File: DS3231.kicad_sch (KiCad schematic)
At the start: 8 parts, among them IC2 DS3231, J4 Conn_01x08_Pin

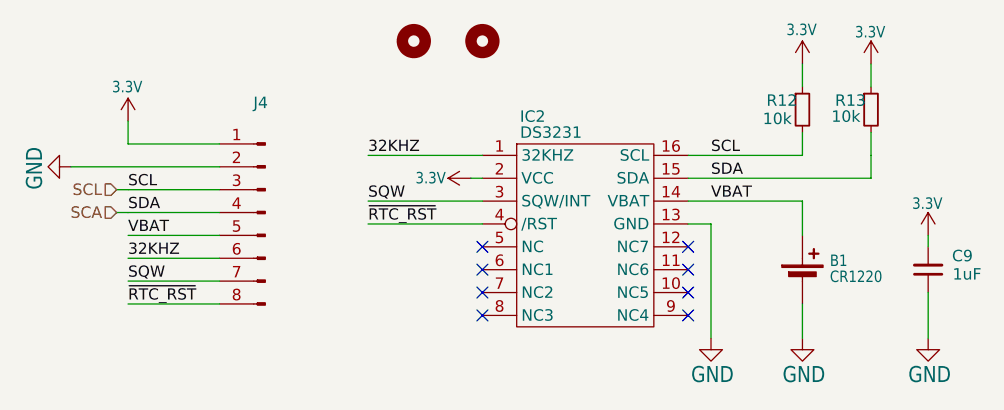
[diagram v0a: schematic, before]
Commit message: added pyrano, anemo, AM2315C, power supply, LEDs, switch and FPC connector in schematic
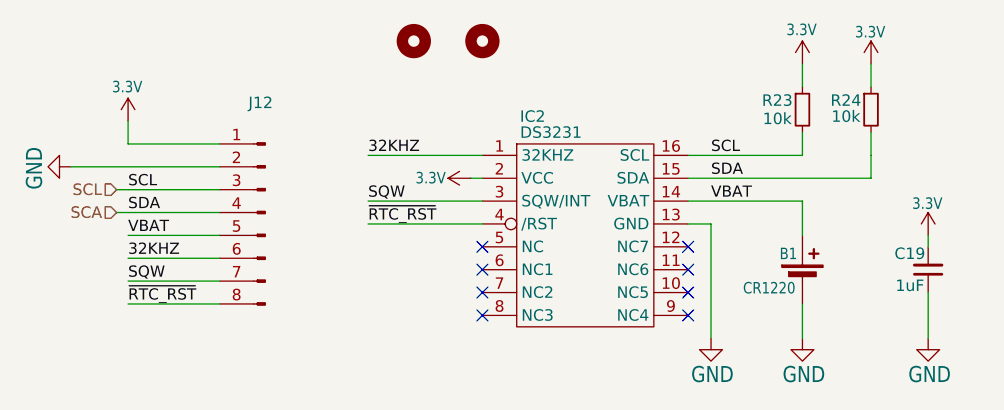
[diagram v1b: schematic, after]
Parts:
- renumbered C9 to C19, J4 to J12, R12 to R23, R13 to R24, U$6 to U$10, U$5 to U$9
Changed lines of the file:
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@@
 		(on_board yes)
 		(dnp no)
-		(property "Reference" "R13"
-			(at 180.594 81.534 0)
+		(property "Reference" "R24"
+			(at 180.086 81.534 0)
 			(effects
 				(font
@@
 			(project "testing-station"
 				(path "/ed3950ec-e24f-4dd6-b9cc-eca012f1333b/7b5dd94c-543e-4c31-b2c6-5bdcb1b32a26"
-					(reference "R13")
+					(reference "R24")
 					(unit 1)
 				)
@@
 		(on_board yes)
 		(dnp no)
-		(property "Reference" "U$6"
+		(property "Reference" "U$10"
 			(at 139.7 74.93 0)
 			(effects
@@
 			(project "testing-station"
 				(path "/ed3950ec-e24f-4dd6-b9cc-eca012f1333b/7b5dd94c-543e-4c31-b2c6-5bdcb1b32a26"
-					(reference "U$6")
+					(reference "U$10")
 					(unit 1)
 				)
@@
 		(on_board yes)
 		(dnp no)
-		(property "Reference" "#U$037"
+		(property "Reference" "#U$067"
 			(at 189.23 96.52 0)
 			(effects
@@
 			(project "testing-station"
 				(path "/ed3950ec-e24f-4dd6-b9cc-eca012f1333b/7b5dd94c-543e-4c31-b2c6-5bdcb1b32a26"
-					(reference "#U$037")
+					(reference "#U$067")
 					(unit 1)
 				)
@@
 		(on_board yes)
 		(dnp no)
-		(property "Reference" "U$5"
+		(property "Reference" "U$9"
 			(at 132.08 74.93 0)
 			(effects
@@
 			(project "testing-station"
 				(path "/ed3950ec-e24f-4dd6-b9cc-eca012f1333b/7b5dd94c-543e-4c31-b2c6-5bdcb1b32a26"
-					(reference "U$5")
+					(reference "U$9")
 					(unit 1)
 				)
@@
 		(on_board yes)
 		(dnp no)
-		(property "Reference" "R12"
-			(at 172.974 81.534 0)
+		(property "Reference" "R23"
+			(at 172.466 81.534 0)
 			(effects
 				(font
@@
 			(project "testing-station"
 				(path "/ed3950ec-e24f-4dd6-b9cc-eca012f1333b/7b5dd94c-543e-4c31-b2c6-5bdcb1b32a26"
-					(reference "R12")
+					(reference "R23")
 					(unit 1)
 				)
@@
 		(on_board yes)
 		(dnp no)
-		(property "Reference" "#U$035"
+		(property "Reference" "#U$065"
 			(at 100.33 83.82 0)
 			(effects
@@
 			(project "testing-station"
 				(path "/ed3950ec-e24f-4dd6-b9cc-eca012f1333b/7b5dd94c-543e-4c31-b2c6-5bdcb1b32a26"
-					(reference "#U$035")
+					(reference "#U$065")
 					(unit 1)
 				)
@@
 		(on_board yes)
 		(dnp no)
-		(property "Reference" "#U$034"
+		(property "Reference" "#U$064"
 			(at 182.88 77.47 0)
 			(effects
@@
 			(project "testing-station"
 				(path "/ed3950ec-e24f-4dd6-b9cc-eca012f1333b/7b5dd94c-543e-4c31-b2c6-5bdcb1b32a26"
-					(reference "#U$034")
+					(reference "#U$064")
 					(unit 1)
 				)
@@
 		(on_board yes)
 		(dnp no)
-		(property "Reference" "#U$036"
+		(property "Reference" "#U$066"
 			(at 138.43 90.17 0)
 			(effects
@@
 			(project "testing-station"
 				(path "/ed3950ec-e24f-4dd6-b9cc-eca012f1333b/7b5dd94c-543e-4c31-b2c6-5bdcb1b32a26"
-					(reference "#U$036")
+					(reference "#U$066")
 					(unit 1)
 				)
@@
 		(on_board yes)
 		(dnp no)
-		(property "Reference" "#U$033"
+		(property "Reference" "#U$063"
 			(at 175.26 77.47 0)
 			(effects
@@
 			(project "testing-station"
 				(path "/ed3950ec-e24f-4dd6-b9cc-eca012f1333b/7b5dd94c-543e-4c31-b2c6-5bdcb1b32a26"
-					(reference "#U$033")
+					(reference "#U$063")
 					(unit 1)
 				)
@@
 		(on_board yes)
 		(dnp no)
-		(property "Reference" "J4"
+		(property "Reference" "J12"
 			(at 115.062 81.788 0)
 			(effects
@@
 			(project "testing-station"
 				(path "/ed3950ec-e24f-4dd6-b9cc-eca012f1333b/7b5dd94c-543e-4c31-b2c6-5bdcb1b32a26"
-					(reference "J4")
+					(reference "J12")
 					(unit 1)
 				)
@@
 		(dnp no)
 		(property "Reference" "B1"
-			(at 178.308 100.076 0)
+			(at 172.72 99.314 0)
 			(effects
 				(font
@@
 		)
 		(property "Value" "CR1220"
-			(at 178.308 101.854 0)
+			(at 168.656 103.124 0)
 			(effects
 				(font
@@
 		(on_board yes)
 		(dnp no)
-		(property "Reference" "C9"
-			(at 193.04 98.806 0)
+		(property "Reference" "C19"
+			(at 187.198 98.552 0)
 			(effects
 				(font
@@
 		)
 		(property "Value" "1uF"
-			(at 193.548 100.838 0)
+			(at 187.198 102.108 0)
 			(effects
 				(font
@@
 			(project "testing-station"
 				(path "/ed3950ec-e24f-4dd6-b9cc-eca012f1333b/7b5dd94c-543e-4c31-b2c6-5bdcb1b32a26"
-					(reference "C9")
-					(unit 1)
-				)
+					(reference "C19")
+					(unit 1)
+				)

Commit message: removed connectors from modules
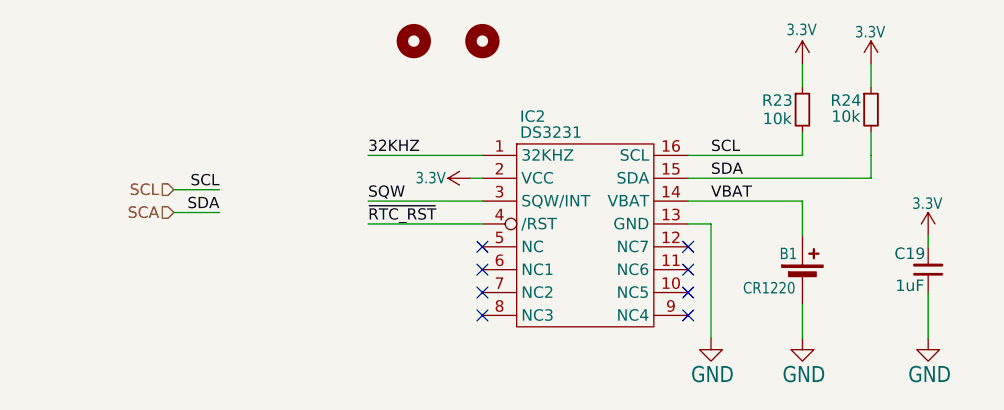
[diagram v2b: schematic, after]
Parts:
- removed J12: Conn_01x08_Pin, Connector_PinHeader_2.54mm:PinHeader_1x08_P2.54mm_Vertical, symbol Connector:Conn_01x08_Pin

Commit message: added DS3231 external files
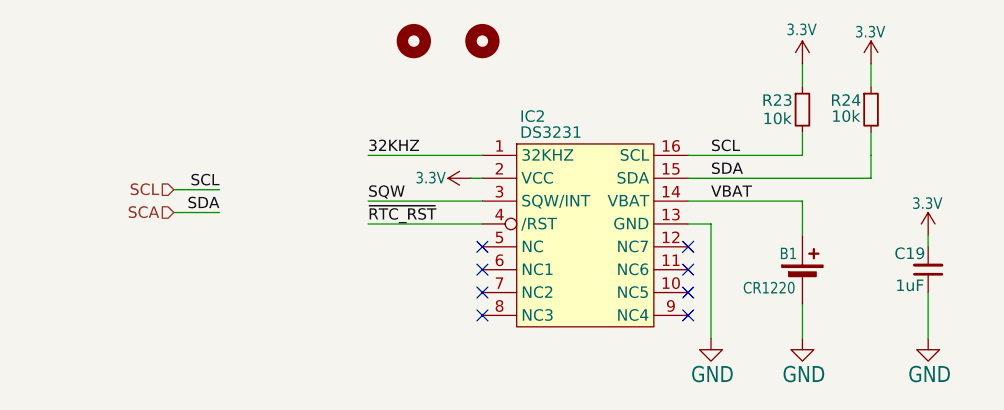
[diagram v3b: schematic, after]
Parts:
- B1: footprint external_footprints:CR1220-SMD -> external_footprints:CR1220
- IC2: symbol external_library:DS3231 -> external_symbols:DS3231
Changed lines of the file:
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@@
 	)
 	(symbol
-		(lib_id "external_library:DS3231")
+		(lib_id "external_symbols:DS3231")
 		(at 143.51 106.68 0)
 		(unit 1)
@@
 			)
 		)
-		(property "Footprint" "external_footprints:CR1220-SMD"
+		(property "Footprint" "external_footprints:CR1220"
 			(at 175.26 100.076 90)
 			(effects

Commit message: removed mouting holes
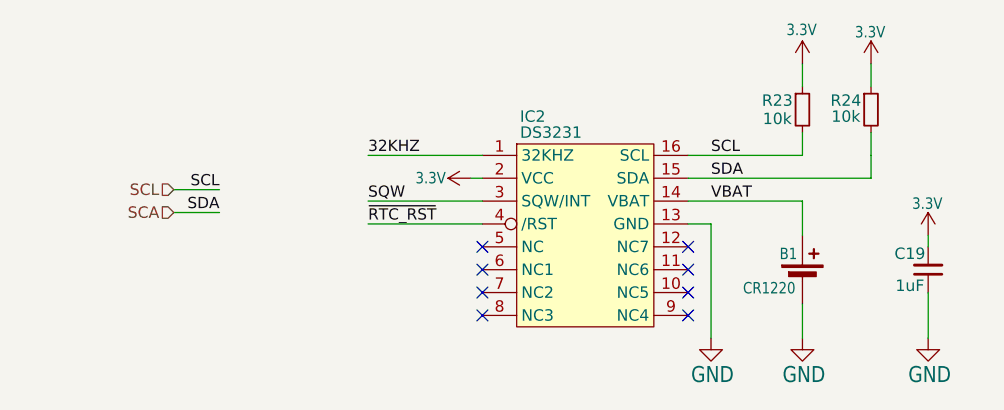
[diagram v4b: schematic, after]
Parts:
- removed U$10, U$9: MOUNTINGHOLE2.5, MountingHole:MountingHole_2.5mm, symbol Mechanical:MountingHole
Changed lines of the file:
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@@
-	)
-	(symbol
-		(lib_id "Mechanical:MountingHole")
-		(at 139.7 74.93 0)
-		(unit 1)
-		(exclude_from_sim no)
-		(in_bom no)
-		(on_board yes)
-		(dnp no)
-		(property "Reference" "U$10"
-			(at 139.7 74.93 0)
-			(effects
-				(font
-					(size 1.27 1.27)
-				)
-				(hide yes)
-			)
-		)
-		(property "Value" "MOUNTINGHOLE2.5"
-			(at 139.7 74.93 0)
-			(effects
-				(font
-					(size 1.27 1.27)
-				)
-				(hide yes)
-			)
-		)
-		(property "Footprint" "MountingHole:MountingHole_2.5mm"
-			(at 139.7 74.93 0)
-			(effects
-				(font
-					(size 1.27 1.27)
-				)
-				(hide yes)
-			)
-		)
-		(property "Datasheet" ""
-			(at 139.7 74.93 0)
-			(effects
-				(font
-					(size 1.27 1.27)
-				)
-				(hide yes)
-			)
-		)
-		(property "Description" "Mounting Hole without connection"
-			(at 139.7 74.93 0)
-			(effects
-				(font
-					(size 1.27 1.27)
-				)
-				(hide yes)
-			)
-		)
-		(instances
-			(project "testing-station"
-				(path "/ed3950ec-e24f-4dd6-b9cc-eca012f1333b/7b5dd94c-543e-4c31-b2c6-5bdcb1b32a26"
-					(reference "U$10")
-					(unit 1)
-				)
-			)
-		)
 	)
 	(symbol
@@
 					(unit 1)
 				)
-			)
-		)
-	)
-	(symbol
-		(lib_id "Mechanical:MountingHole")
-		(at 132.08 74.93 0)
-		(unit 1)
-		(exclude_from_sim no)
-		(in_bom no)
-		(on_board yes)
-		(dnp no)
-		(property "Reference" "U$9"
-			(at 132.08 74.93 0)
-			(effects
-				(font
-					(size 1.27 1.27)
-				)
-				(hide yes)
-			)
-		)
-		(property "Value" "MOUNTINGHOLE2.5"
-			(at 132.08 74.93 0)
-			(effects
-				(font
-					(size 1.27 1.27)
-				)
-				(hide yes)
-			)
-		)
-		(property "Footprint" "MountingHole:MountingHole_2.5mm"
-			(at 132.08 74.93 0)
-			(effects
-				(font
-					(size 1.27 1.27)
-				)
-				(hide yes)
-			)
-		)
-		(property "Datasheet" ""
-			(at 132.08 74.93 0)
-			(effects
-				(font
-					(size 1.27 1.27)
-				)
-				(hide yes)
-			)
-		)
-		(property "Description" "Mounting Hole without connection"
-			(at 132.08 74.93 0)
-			(effects
-				(font
-					(size 1.27 1.27)
-				)
-				(hide yes)
-			)
-		)
-		(instances
-			(project "testing-station"
-				(path "/ed3950ec-e24f-4dd6-b9cc-eca012f1333b/7b5dd94c-543e-4c31-b2c6-5bdcb1b32a26"
-					(reference "U$9")
-					(unit 1)
-				)

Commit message: removed voltage regulators of each individual module
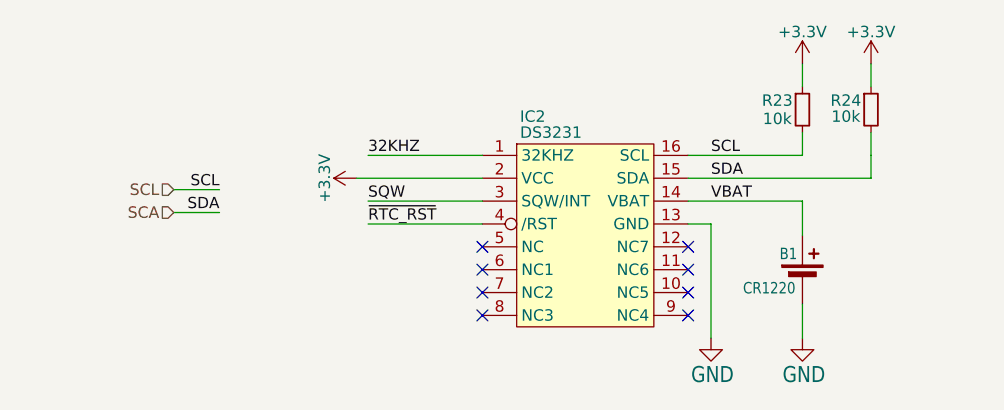
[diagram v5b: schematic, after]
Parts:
- removed C19: 1uF, Capacitor_SMD:C_0805_2012Metric, symbol Device:C_Small
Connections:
- net 3.3V renamed +3.3V

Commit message: DS3231 routed on PCB
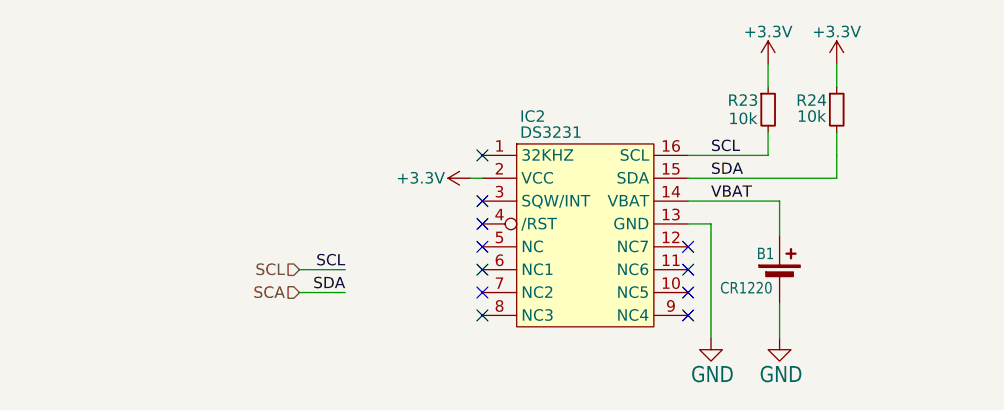
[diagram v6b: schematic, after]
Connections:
- net 32KHZ: no longer names the net of IC2.1 (32KHZ)
- net SQW: no longer names the net of IC2.3 (SQW/INT)
- net ~{RTC_RST}: no longer names the net of IC2.4 (/RST)
- no-connect marks 8 -> 11
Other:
- moved on the sheet: B1, R23, R24

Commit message: BOM update
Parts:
- B1, IC2: Component package type / -> (none)
- R23, R24: Component package type R_0805 -> (none)
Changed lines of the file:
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@@
-			)
-		)
-		(property "Component package type" "R_0805"
-			(at 179.07 82.55 0)
-			(effects
-				(font
-					(size 1.27 1.27)
-				)
-				(hide yes)
 			)
 		)
@@
 			)
 		)
-		(property "Component package type" "R_0805"
-			(at 171.45 82.55 0)
-			(effects
-				(font
-					(size 1.27 1.27)
-				)
-				(hide yes)
-			)
-		)
 		(pin "1"
 		)
@@
 			)
 		)
-		(property "Component package type" "/"
-			(at 143.51 106.68 0)
-			(effects
-				(font
-					(size 1.27 1.27)
-				)
-				(hide yes)
-			)
-		)
 		(pin "1"
 		)
@@
 			(at 172.72 101.6 0)
 			(effects
-				(font
-					(size 1.27 1.27)
-				)
-				(hide yes)
-			)
-		)
-		(property "Component package type" "/"
-			(at 172.72 101.6 0)
-			(effects
